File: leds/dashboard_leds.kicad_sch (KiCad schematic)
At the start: 35 parts, among them J1 Harness, J2 Buttons, J3 Expansion Connector, Q1 2N7002, Q2 2N7002, Q3 2N7002, U1 74LVC3G17, U2 AL5809, U3 AL5809, U4 AL5809, U5 AL5809, U6 AL5809

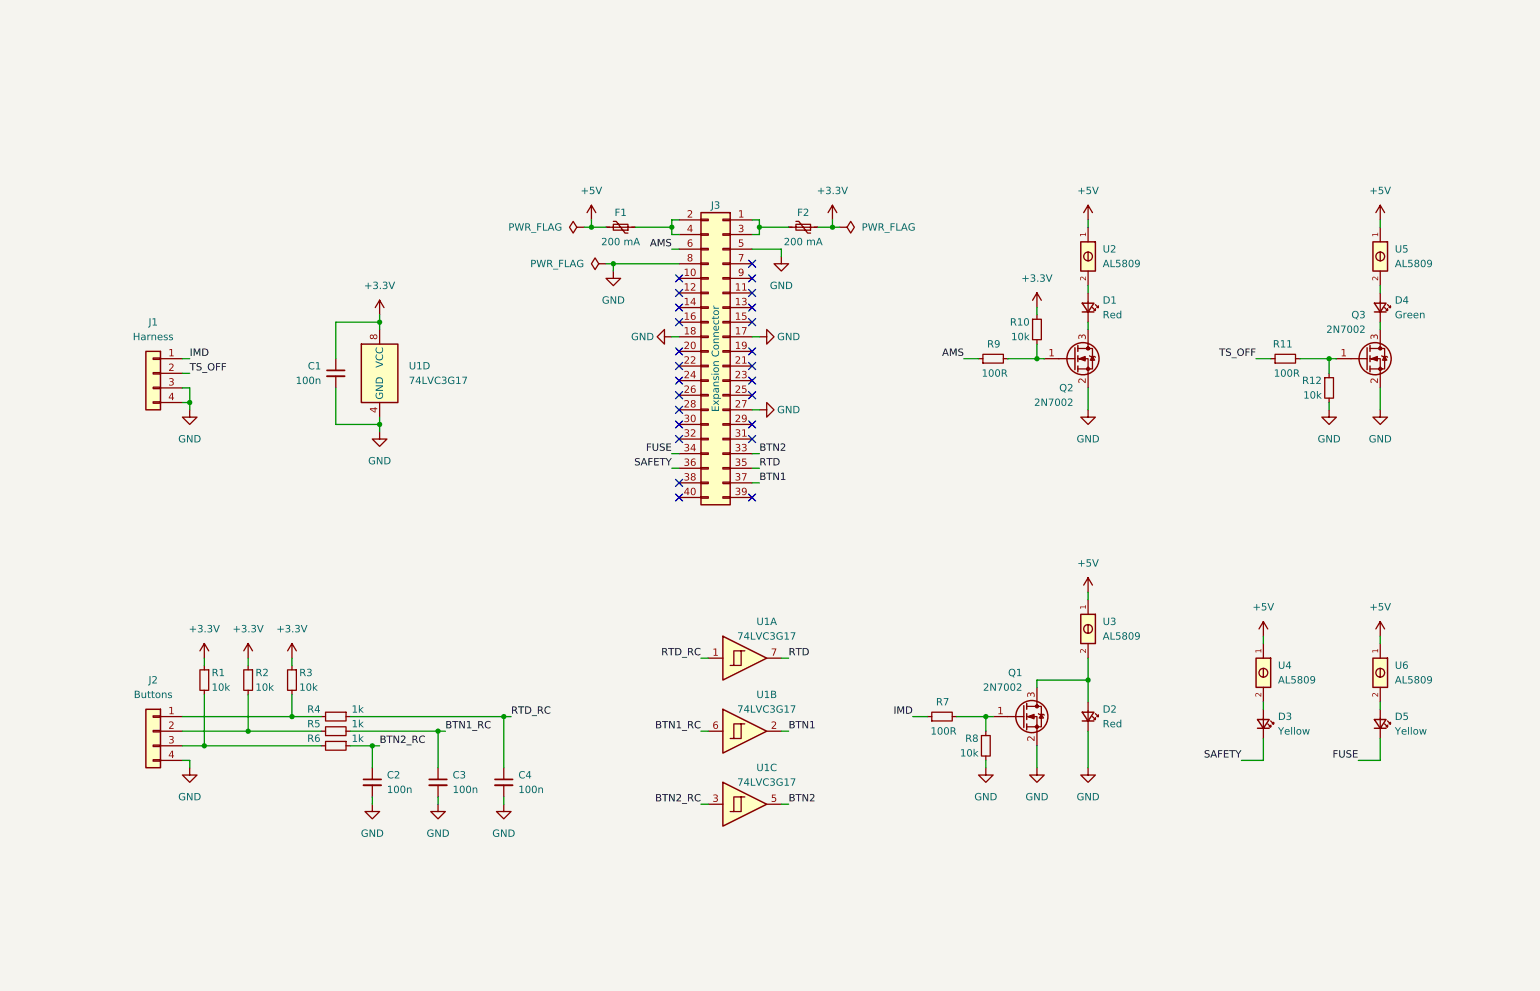
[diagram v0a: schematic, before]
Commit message: Fix connector wiring
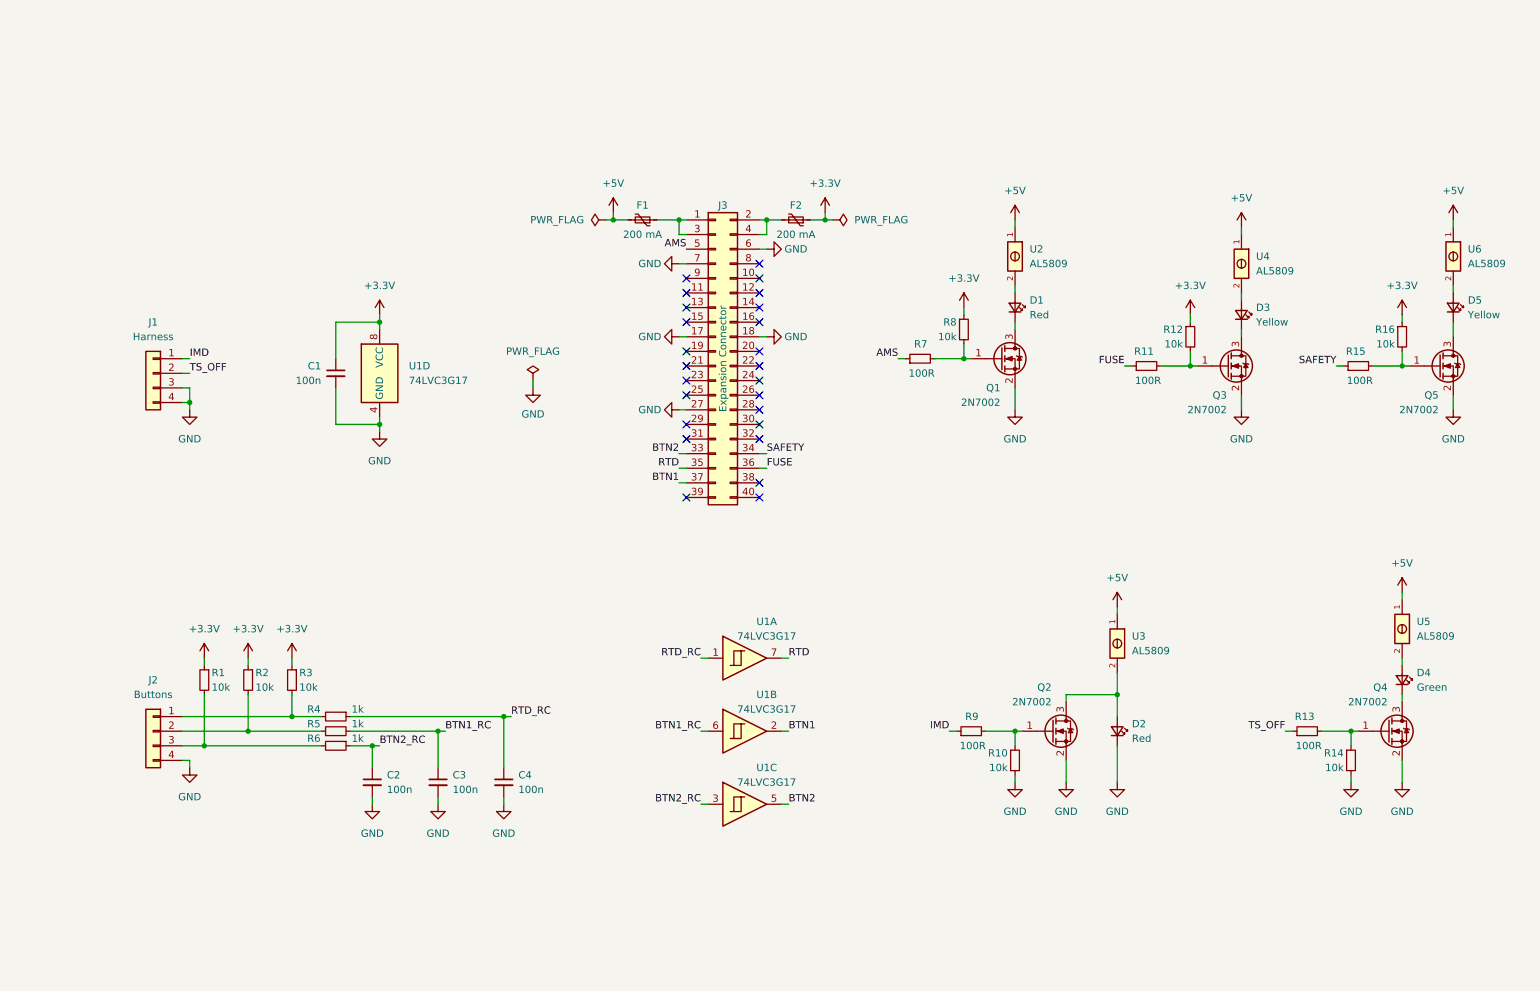
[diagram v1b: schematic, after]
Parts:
- added Q3, Q5: 2N7002, Package_TO_SOT_SMD:SOT-23, symbol Transistor_FET:2N7002
- added R11, R15: 100R, Resistor_SMD:R_0603_1608Metric, symbol Device:R_Small
- added R12, R16: 10k, Resistor_SMD:R_0603_1608Metric, symbol Device:R_Small
- renumbered Q2 to Q1, Q1 to Q2, Q3 to Q4, R8 to R10, R11 to R13, R12 to R14, R9 to R7, R10 to R8, R7 to R9
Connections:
- net +3.3V: now also R12.1, R16.1
- net AMS: now also J3.5 (Pin_5); no longer J3.6 (Pin_6)
- net FUSE: now also J3.36 (Pin_36), R11.1; no longer D5.1 (K), J3.34 (Pin_34)
- net GND: now also J3.6 (Pin_6), J3.7 (Pin_7), Q3.2 (S), Q5.2 (S); no longer J3.5 (Pin_5), J3.8 (Pin_8)
- net SAFETY: now also J3.34 (Pin_34), R15.1; no longer D3.1 (K), J3.36 (Pin_36)
- net at J3.1 (Pin_1), J3.3 (Pin_3): now also F1.1; no longer F2.2
- net at J3.2 (Pin_2), J3.4 (Pin_4): now also F2.2; no longer F1.1
- new net: Q5.1 (G), R15.2, R16.2
- new net: D5.1 (K), Q5.3 (D)
- new net: Q3.1 (G), R11.2, R12.2
- new net: D3.1 (K), Q3.3 (D)
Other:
- moved on the sheet: D1, D2, D3, D4, D5, F1, F2, J3, Q1, Q2, Q4, R10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

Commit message: Update button labels
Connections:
- net BTN1 renamed TSA_BTN
- net BTN1_RC renamed TSA_BTN_RC
- net BTN2 renamed USR_BTN
- net BTN2_RC renamed USR_BTN_RC
- net FUSE renamed FUSE_LED
- net RTD renamed RTD_BTN
- net SAFETY renamed SAFETY_LED
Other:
- moved on the sheet: C3, C4, D1, D3, D5, Q1, Q3, Q5, R11, R12, R15, R16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

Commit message: Edit the scheme
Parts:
- removed J2: Buttons, Local_Library:SolderWire-0.15sqmm_Relief, symbol Connector_Generic:Conn_01x04
- removed U1: 74LVC3G17, Local_Library:74LVC3G17, symbol 74LVC3G17:74LVC3G17
- removed U2, U3, U4, U5, U6: AL5809, Local_Library:AL5809-20QP1-7, symbol AL5809:AL5809-20QP1-7
- added C5: 1u, Capacitor_SMD:C_0603_1608Metric, symbol Device:C_Small
- added J2: Conn_01x06, Connector_Wire:SolderWire-0.15sqmm_1x06_P4mm_D0.5mm_OD1.5mm_Relief, symbol Connector_Generic:Conn_01x06
- added R17, R18, R19, R20, R21: 140, Resistor_SMD:R_1206_3216Metric, symbol Device:R_Small
- added R22, R23: 1k, Resistor_SMD:R_0603_1608Metric, symbol Device:R_Small
- added R24, R25: 10k, Resistor_SMD:R_0603_1608Metric, symbol Device:R_Small
- C1, C2, C3, C4: value 100n -> 1u
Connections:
- net RTD_RC is gone; now on net RTD_BTN: C4.1, R4.1
- net TSA_BTN_RC is gone; now on net TSA_BTN: C3.1, R5.2
- net +3.3V: now also R24.1, R25.1; no longer C1.1
- net +5V: now also R17.1, R18.1, R19.1, R20.1, R21.1
- net GND: now also C5.2, J2.1 (Pin_1)
- net USR_BTN: now also J3.24 (Pin_24), C5.1, R22.1; no longer J3.33 (Pin_33)
- net at D2.2 (A), Q2.3 (D): now also R21.2
- net at R2.2, R5.1: now also J2.3 (Pin_3)
- net at R3.2, R4.2: now also J2.4 (Pin_4)
- net at R1.2, R6.2: now also J2.2 (Pin_2)
- net at D5.2 (A): now also R19.2
- net at D1.2 (A): now also R17.2
- net at D4.2 (A): now also R20.2
- net at D3.2 (A): now also R18.2
- net DRS_BTN: now reaches J3.26 (Pin_26)
- net DRS_BTN: now also C1.1, R23.1
- net USR_BTN_RC renamed CS_BTN
- net CS_BTN: now also J3.33 (Pin_33)
- new net: J2.6 (Pin_6), R22.2, R25.2
- new net: J2.5 (Pin_5), R23.2, R24.2
- no-connect marks 25 -> 23
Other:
- note added: "Buttons"
- note added: "Connector"
- note added: "LED'S"
- company: Author: I. Kajdan -> Author: I. Kajdan & Michał Błotniak
- moved on the sheet: C2, C3, C4, D1, D2, D3, D4, D5, F1, F2, J1, J3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

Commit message: Edit PCB layout
*without zone
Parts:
- R17, R18, R19, R20, R21: footprint Resistor_SMD:R_1206_3216Metric -> Resistor_SMD:R_0805_2012Metric
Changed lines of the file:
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@@
 			)
 		)
-		(property "Footprint" "Resistor_SMD:R_1206_3216Metric"
+		(property "Footprint" "Resistor_SMD:R_0805_2012Metric"
 			(at 146.05 38.1 0)
 			(effects
@@
 			)
 		)
-		(property "Footprint" "Resistor_SMD:R_1206_3216Metric"
+		(property "Footprint" "Resistor_SMD:R_0805_2012Metric"
 			(at 248.92 36.83 0)
 			(effects
@@
 			)
 		)
-		(property "Footprint" "Resistor_SMD:R_1206_3216Metric"
+		(property "Footprint" "Resistor_SMD:R_0805_2012Metric"
 			(at 199.39 39.37 0)
 			(effects
@@
 			)
 		)
-		(property "Footprint" "Resistor_SMD:R_1206_3216Metric"
+		(property "Footprint" "Resistor_SMD:R_0805_2012Metric"
 			(at 57.15 38.1 0)
 			(effects
@@
 			)
 		)
-		(property "Footprint" "Resistor_SMD:R_1206_3216Metric"
+		(property "Footprint" "Resistor_SMD:R_0805_2012Metric"
 			(at 96.52 36.83 0)
 			(effects

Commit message: Fixing bugs on PCB
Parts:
- R17, R18, R19, R20, R21: value 140 -> 150
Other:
- note added: "IMD & TS Connector"
- moved on the sheet: J1
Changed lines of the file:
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@@
 	)
 	(junction
-		(at 110.49 106.68)
+		(at 54.61 104.14)
 		(diameter 0)
 		(color 0 0 0 0)
@@
 	(wire
 		(pts
-			(xy 110.49 106.68) (xy 109.22 106.68)
+			(xy 54.61 104.14) (xy 53.34 104.14)
 		)
 		(stroke
@@
 	(wire
 		(pts
-			(xy 110.49 104.14) (xy 110.49 106.68)
+			(xy 54.61 101.6) (xy 54.61 104.14)
 		)
 		(stroke
@@
 	(wire
 		(pts
-			(xy 110.49 106.68) (xy 110.49 107.95)
+			(xy 54.61 104.14) (xy 54.61 105.41)
 		)
 		(stroke
@@
 	(wire
 		(pts
-			(xy 109.22 101.6) (xy 110.49 101.6)
+			(xy 53.34 99.06) (xy 54.61 99.06)
 		)
 		(stroke
@@
 	(wire
 		(pts
-			(xy 109.22 104.14) (xy 110.49 104.14)
+			(xy 53.34 101.6) (xy 54.61 101.6)
 		)
 		(stroke
@@
 	(wire
 		(pts
-			(xy 127 101.6) (xy 127 102.87)
+			(xy 191.77 142.24) (xy 191.77 143.51)
 		)
 		(stroke
@@
 	(wire
 		(pts
-			(xy 110.49 99.06) (xy 109.22 99.06)
+			(xy 54.61 96.52) (xy 53.34 96.52)
 		)
 		(stroke
@@
 	)
 	(rectangle
+		(start 26.67 86.36)
+		(end 76.2 115.57)
+		(stroke
+			(width 0)
+			(type default)
+		)
+		(fill
+			(type none)
+		)
+	)
+	(rectangle
 		(start 25.4 133.35)
 		(end 166.37 182.88)
@@
 	)
 	(rectangle
-		(start 184.15 90.17)
+		(start 182.88 90.17)
 		(end 262.89 158.75)
 		(stroke
@@
 		)
 	)
+	(text "IMD & TS Connector"
+		(exclude_from_sim no)
+		(at 65.024 82.55 0)
+		(effects
+			(font
+				(size 5.08 5.08)
+			)
+		)
+	)
 	(label "IMD"
 		(at 170.18 54.61 180)
@@
 	)
 	(label "IMD"
-		(at 110.49 99.06 0)
+		(at 54.61 96.52 0)
 		(fields_autoplaced yes)
 		(effects
@@
 	)
 	(label "TS_OFF"
-		(at 110.49 101.6 0)
+		(at 54.61 99.06 0)
 		(fields_autoplaced yes)
 		(effects
@@
 			)
 		)
-		(property "Value" "140"
+		(property "Value" "150"
 			(at 148.59 39.3699 0)
 			(effects
@@
 	(symbol
 		(lib_id "power:PWR_FLAG")
-		(at 127 101.6 0)
+		(at 191.77 142.24 0)
 		(mirror y)
 		(unit 1)
@@
 		(fields_autoplaced yes)
 		(property "Reference" "#FLG01"
-			(at 127 99.695 0)
+			(at 191.77 140.335 0)
 			(effects
 				(font
@@
 		)
 		(property "Value" "PWR_FLAG"
-			(at 127 96.52 0)
+			(at 191.77 137.16 0)
 			(effects
 				(font
@@
 		)
 		(property "Footprint" ""
-			(at 127 101.6 0)
+			(at 191.77 142.24 0)
 			(effects
 				(font
@@
 		)
 		(property "Datasheet" "~"
-			(at 127 101.6 0)
+			(at 191.77 142.24 0)
 			(effects
 				(font
@@
 		)
 		(property "Description" "Special symbol for telling ERC where power comes from"
-			(at 127 101.6 0)
+			(at 191.77 142.24 0)
 			(effects
 				(font
@@
 			)
 		)
-		(property "Value" "140"
+		(property "Value" "150"
 			(at 251.46 38.0999 0)
 			(effects
@@
 	(symbol
 		(lib_id "power:GND")
-		(at 127 102.87 0)
+		(at 191.77 143.51 0)
 		(unit 1)
 		(exclude_from_sim no)
@@
 		(dnp no)
 		(property "Reference" "#PWR010"
-			(at 127 109.22 0)
+			(at 191.77 149.86 0)
 			(effects
 				(font
@@
 		)
 		(property "Value" "GND"
-			(at 127 107.442 0)
+			(at 191.77 148.082 0)
 			(effects
 				(font
@@
 		)
 		(property "Footprint" ""
-			(at 127 102.87 0)
+			(at 191.77 143.51 0)
 			(effects
 				(font
@@
 		)
 		(property "Datasheet" ""
-			(at 127 102.87 0)
+			(at 191.77 143.51 0)
 			(effects
 				(font
@@
 		)
 		(property "Description" "Power symbol creates a global label with name \"GND\" , ground"
-			(at 127 102.87 0)
+			(at 191.77 143.51 0)
 			(effects
 				(font
@@
 			)
 		)
-		(property "Value" "140"
+		(property "Value" "150"
 			(at 201.93 40.6399 0)
 			(effects
@@
 	(symbol
 		(lib_id "power:GND")
-		(at 110.49 107.95 0)
+		(at 54.61 105.41 0)
 		(unit 1)
 		(exclude_from_sim no)
@@
 		(dnp no)
 		(property "Reference" "#PWR01"
-			(at 110.49 114.3 0)
+			(at 54.61 111.76 0)
 			(effects
 				(font
@@
 		)
 		(property "Value" "GND"
-			(at 110.49 113.03 0)
+			(at 54.61 110.49 0)
 			(effects
 				(font
@@
 		)
 		(property "Footprint" ""
-			(at 110.49 107.95 0)
+			(at 54.61 105.41 0)
 			(effects
 				(font
@@
 		)
 		(property "Datasheet" ""
-			(at 110.49 107.95 0)
+			(at 54.61 105.41 0)
 			(effects
 				(font
@@
 		)
 		(property "Description" "Power symbol creates a global label with name \"GND\" , ground"
-			(at 110.49 107.95 0)
+			(at 54.61 105.41 0)
 			(effects
 				(font
@@
 			)
 		)
-		(property "Value" "140"
+		(property "Value" "150"
 			(at 59.69 39.3699 0)
 			(effects
@@
 	(symbol
 		(lib_id "Connector_Generic:Conn_01x04")
-		(at 104.14 101.6 0)
+		(at 48.26 99.06 0)
 		(mirror y)
 		(unit 1)
@@
 		(fields_autoplaced yes)
 		(property "Reference" "J1"
-			(at 104.14 92.71 0)
+			(at 48.26 90.17 0)
 			(effects
 				(font
@@
 		)
 		(property "Value" "Harness"
-			(at 104.14 95.25 0)
+			(at 48.26 92.71 0)
 			(effects
 				(font
@@
 		)
 		(property "Footprint" "Local_Library:Molex_53261-0471"
-			(at 104.14 101.6 0)
+			(at 48.26 99.06 0)
 			(effects
 				(font
@@
 		)
 		(property "Datasheet" "https://www.molex.com/en-us/products/part-detail/532610471?display=pdf"
-			(at 104.14 101.6 0)
+			(at 48.26 99.06 0)
 			(effects
 				(font
@@
 		)
 		(property "Description" ""
-			(at 104.14 101.6 0)
+			(at 48.26 99.06 0)
 			(effects
 				(font
@@
 		)
 		(property "Component" " 538-53261-0471"
-			(at 104.14 101.6 0)
+			(at 48.26 99.06 0)
 			(effects
 				(font
@@
 			)
 		)
-		(property "Value" "140"
+		(property "Value" "150"
 			(at 99.06 38.0999 0)
 			(effects

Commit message: Editing zones and minor changes
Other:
- note added: "150/200 mW"
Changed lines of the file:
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@@
+		)
+	)
+	(text "150/200 mW"
+		(exclude_from_sim no)
+		(at 49.276 36.322 0)
+		(effects
+			(font
+				(size 1.27 1.27)
+			)
+		)
+	)
+	(text "150/200 mW"
+		(exclude_from_sim no)
+		(at 191.516 36.576 0)
+		(effects
+			(font
+				(size 1.27 1.27)
+			)
 		)
 	)
@@
 			)
 		)
+	)
+	(text "150/200 mW"
+		(exclude_from_sim no)
+		(at 240.792 35.306 0)
+		(effects
+			(font
+				(size 1.27 1.27)
+			)
+		)
+	)
+	(text "150/200 mW"
+		(exclude_from_sim no)
+		(at 138.43 35.56 0)
+		(effects
+			(font
+				(size 1.27 1.27)
+			)
+		)
+	)
+	(text "150/200 mW"
+		(exclude_from_sim no)
+		(at 88.646 35.56 0)
+		(effects
+			(font
+				(size 1.27 1.27)
+			)
+		)

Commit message: Complete change of design
Change from 2 layer to 4 layer, add bigger resistors, change diodes
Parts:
- D1, D2, D3, D4, D5: footprint Local_Library:Wurth_Elektronik_150224 -> LED_SMD:LED_PLCC-2_3.4x3.0mm_AK
- Q1, Q2, Q3, Q4, Q5: value 2N7002 -> BSS138
- R17, R18, R19, R21: footprint Resistor_SMD:R_0805_2012Metric -> Resistor_SMD:R_1206_3216Metric
- R20: value 150 -> 100; footprint Resistor_SMD:R_0805_2012Metric -> Resistor_SMD:R_1206_3216Metric
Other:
- note added: "100 mW"
- note removed: "150/200 mW"
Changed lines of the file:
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@@
 		)
 	)
-	(text "Connector"
+	(text "100 mW"
 		(exclude_from_sim no)
-		(at 202.438 86.36 0)
+		(at 242.57 34.544 0)
 		(effects
 			(font
-				(size 5.08 5.08)
+				(size 1.27 1.27)
 			)
 		)
 	)
-	(text "150/200 mW"
+	(text "100 mW"
 		(exclude_from_sim no)
-		(at 49.276 36.322 0)
+		(at 139.446 35.56 0)
 		(effects
 			(font
@@
 		)
 	)
-	(text "150/200 mW"
+	(text "Connector"
+		(exclude_from_sim no)
+		(at 202.438 86.36 0)
+		(effects
+			(font
+				(size 5.08 5.08)
+			)
+		)
+	)
+	(text "100 mW"
 		(exclude_from_sim no)
-		(at 191.516 36.576 0)
+		(at 49.276 36.322 0)
 		(effects
 			(font
@@
 		)
 	)
-	(text "150/200 mW"
+	(text "100 mW"
 		(exclude_from_sim no)
-		(at 240.792 35.306 0)
+		(at 193.294 36.322 0)
 		(effects
 			(font
@@
 		)
 	)
-	(text "150/200 mW"
+	(text "IMD & TS Connector"
 		(exclude_from_sim no)
-		(at 138.43 35.56 0)
+		(at 65.024 82.55 0)
 		(effects
 			(font
-				(size 1.27 1.27)
+				(size 5.08 5.08)
 			)
 		)
 	)
-	(text "150/200 mW"
+	(text "100 mW"
 		(exclude_from_sim no)
-		(at 88.646 35.56 0)
+		(at 89.916 35.306 0)
 		(effects
 			(font
@@
 		)
 	)
-	(text "IMD & TS Connector"
-		(exclude_from_sim no)
-		(at 65.024 82.55 0)
-		(effects
-			(font
-				(size 5.08 5.08)
-			)
-		)
-	)
 	(label "IMD"
 		(at 170.18 54.61 180)
@@
 			)
 		)
-		(property "Value" "2N7002"
+		(property "Value" "BSS138"
 			(at 143.51 63.5 0)
 			(effects
@@
 			)
 		)
-		(property "Value" "2N7002"
+		(property "Value" "BSS138"
 			(at 187.96 49.53 0)
 			(effects
@@
 			)
 		)
-		(property "Footprint" "Resistor_SMD:R_0805_2012Metric"
+		(property "Footprint" "Resistor_SMD:R_1206_3216Metric"
 			(at 146.05 38.1 0)
 			(effects
@@
 		)
 		(instances
-			(project ""
+			(project "dashboard_leds"
 				(path "/b652b05a-4e3d-4ad1-b032-18886abe7d45"
 					(reference "R17")
@@
 			)
 		)
-		(property "Value" "150"
+		(property "Value" "100"
 			(at 251.46 38.0999 0)
 			(effects
@@
 			)
 		)
-		(property "Footprint" "Resistor_SMD:R_0805_2012Metric"
+		(property "Footprint" "Resistor_SMD:R_1206_3216Metric"
 			(at 248.92 36.83 0)
 			(effects
@@
 			)
 		)
-		(property "Value" "2N7002"
+		(property "Value" "BSS138"
 			(at 93.98 63.5 0)
 			(effects
@@
 			)
 		)
-		(property "Value" "2N7002"
+		(property "Value" "BSS138"
 			(at 246.38 49.53 0)
 			(effects
@@
 			)
 		)
-		(property "Footprint" "Local_Library:Wurth_Elektronik_150224"
+		(property "Footprint" "LED_SMD:LED_PLCC-2_3.4x3.0mm_AK"
 			(at 96.52 45.72 90)
 			(effects
@@
 			)
 		)
-		(property "Datasheet" "https://www.we-online.com/components/products/datasheet/150224YS73100A.pdf"
+		(property "Datasheet" "https://www.tme.eu/Document/b727a26c2a14c1b978f399fc0d48d055/RF-YURA30TS-AE.pdf"
 			(at 96.52 45.72 90)
 			(effects
@@
 			)
 		)
-		(property "Footprint" "Resistor_SMD:R_0805_2012Metric"
+		(property "Footprint" "Resistor_SMD:R_1206_3216Metric"
 			(at 199.39 39.37 0)
 			(effects
@@
 			)
 		)
-		(property "Footprint" "Local_Library:Wurth_Elektronik_150224"
+		(property "Footprint" "LED_SMD:LED_PLCC-2_3.4x3.0mm_AK"
 			(at 248.92 45.72 90)
 			(effects
@@
 			)
 		)
-		(property "Datasheet" "https://www.we-online.com/components/products/datasheet/150224VS73100A.pdf"
+		(property "Datasheet" "https://www.tme.eu/Document/ff2f725a7265a0e46cf1b59e09e8dc43/RF-GNRA30TS-CF.pdf"
 			(at 248.92 45.72 90)
 			(effects
@@
 			)
 		)
-		(property "Value" "2N7002"
+		(property "Value" "BSS138"
 			(at 54.61 63.5 0)
 			(effects
@@
 			)
 		)
-		(property "Footprint" "Local_Library:Wurth_Elektronik_150224"
+		(property "Footprint" "LED_SMD:LED_PLCC-2_3.4x3.0mm_AK"
 			(at 57.15 46.99 90)
 			(effects
@@
 			)
 		)
-		(property "Datasheet" "https://www.we-online.com/components/products/datasheet/150224YS73100A.pdf"
+		(property "Datasheet" "https://www.tme.eu/Document/b727a26c2a14c1b978f399fc0d48d055/RF-YURA30TS-AE.pdf"
 			(at 57.15 46.99 90)
 			(effects
@@
 			)
 		)
-		(property "Footprint" "Local_Library:Wurth_Elektronik_150224"
+		(property "Footprint" "LED_SMD:LED_PLCC-2_3.4x3.0mm_AK"
 			(at 146.05 46.99 90)
 			(effects
@@
 			)
 		)
-		(property "Datasheet" "https://www.we-online.com/components/products/datasheet/150224RS73100A.pdf"
+		(property "Datasheet" "https://www.tme.eu/Document/847253aff8a1c320c4ee0f8f7453c0d2/RF-RURA30TS-CE.pdf"
 			(at 146.05 46.99 90)
 			(effects
@@
 			)
 		)
-		(property "Footprint" "Resistor_SMD:R_0805_2012Metric"
+		(property "Footprint" "Resistor_SMD:R_1206_3216Metric"
 			(at 57.15 38.1 0)
 			(effects
@@
 			)
 		)
-		(property "Footprint" "Local_Library:Wurth_Elektronik_150224"
+		(property "Footprint" "LED_SMD:LED_PLCC-2_3.4x3.0mm_AK"
 			(at 199.39 54.61 90)
 			(effects
@@
 			)
 		)
-		(property "Datasheet" "https://www.we-online.com/components/products/datasheet/150224RS73100A.pdf"
+		(property "Datasheet" "https://www.tme.eu/Document/847253aff8a1c320c4ee0f8f7453c0d2/RF-RURA30TS-CE.pdf"
 			(at 199.39 54.61 90)
 			(effects
@@
 		)
 		(instances
-			(project ""
+			(project "dashboard_leds"
 				(path "/b652b05a-4e3d-4ad1-b032-18886abe7d45"
 					(reference "J2")
@@
 			)
 		)
-		(property "Footprint" "Resistor_SMD:R_0805_2012Metric"
+		(property "Footprint" "Resistor_SMD:R_1206_3216Metric"
 			(at 96.52 36.83 0)
 			(effects

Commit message: Changing the path guidance
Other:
- company: Author: I. Kajdan & Michał Błotniak -> Author:  Michał Błotniak
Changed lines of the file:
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@@
 		(date "2024-11-25")
 		(rev "${REVISION}")
-		(company "Author: I. Kajdan & Michał Błotniak")
+		(company "Author:  Michał Błotniak")
 		(comment 1 "Reviewer:")
 	)
